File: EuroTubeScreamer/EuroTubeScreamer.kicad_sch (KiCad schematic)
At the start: 49 parts, among them Q1 2N3904, Q2 2N3904, U1 RC4558

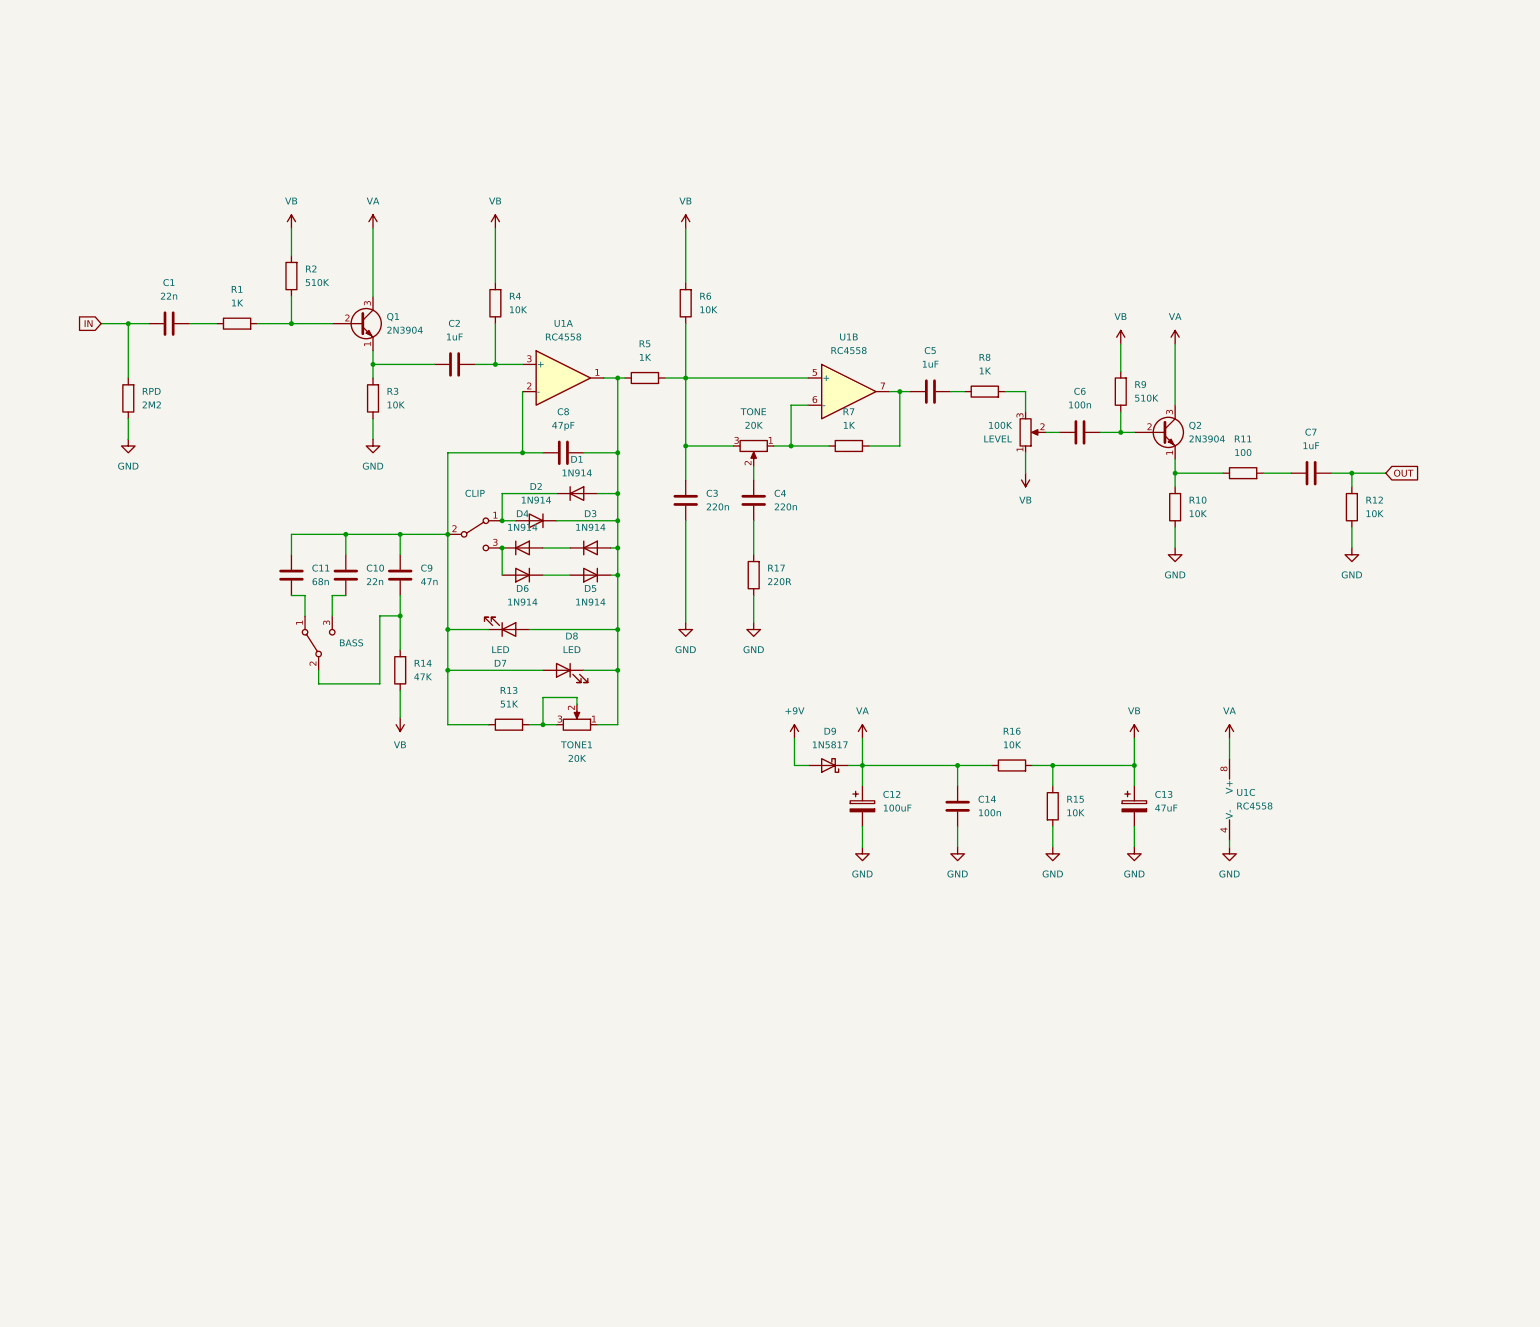
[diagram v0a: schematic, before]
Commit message: added bypass board to schematic and made a start on a panel layout
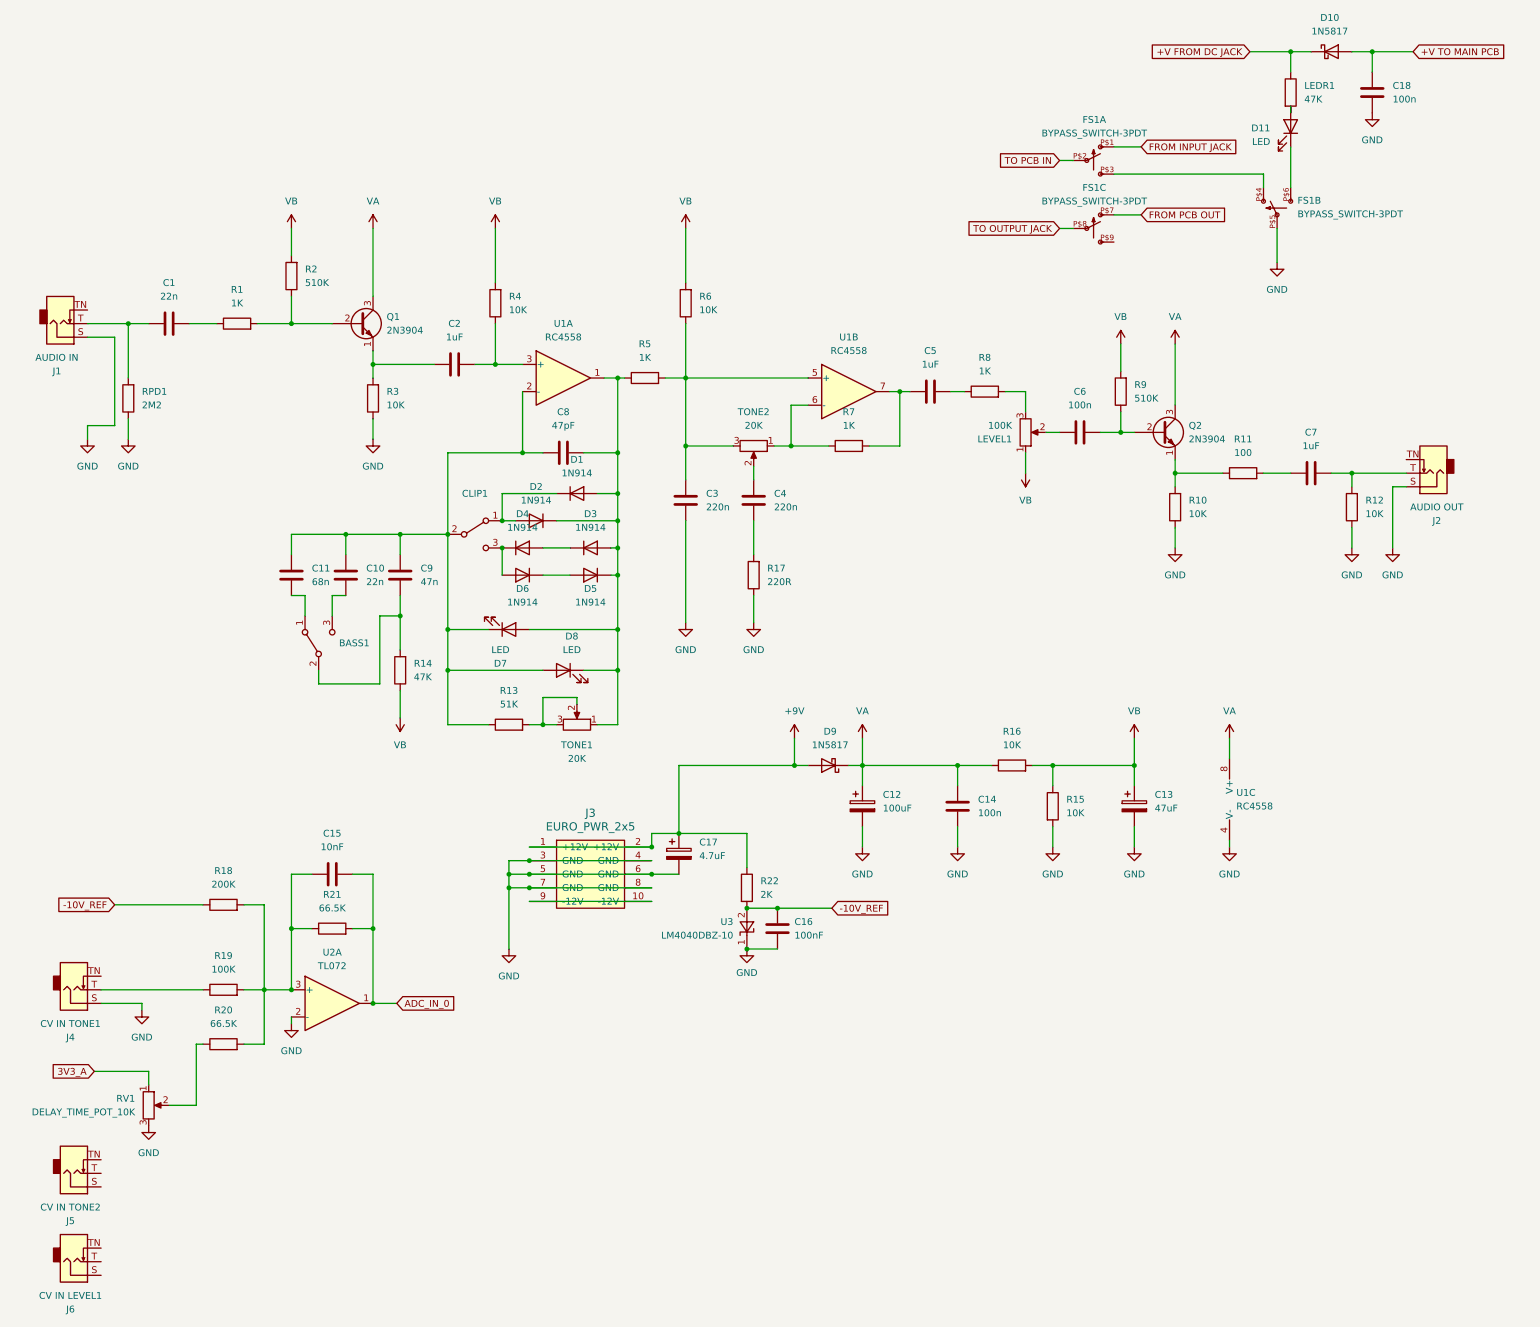
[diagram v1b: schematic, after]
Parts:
- added C15: 10nF, symbol Device:C
- added C16: 100nF, symbol Device:C
- added C17: 4.7uF, Capacitor_THT:CP_Radial_D5.0mm_P2.50mm, symbol Device:C_Polarized
- added C18: 100n, symbol Device:C
- added D10: 1N5817, Diode_THT:D_DO-41_SOD81_P10.16mm_Horizontal, symbol Diode:1N5817
- added D11: LED, LED_THT:LED_D3.0mm, symbol Device:LED
- added FS1: BYPASS_SWITCH-3PDT, SparkFun-Electromechanical:STOMP-SWITCH-3PDT, symbol SparkSparkFun-Electromechanicalfun:SWITCH-3PDT
- added J1: AUDIO IN, eurocad:PJ301M-12_T_S, symbol Connector_Audio:AudioJack2_SwitchT
- added J2: AUDIO OUT, eurocad:PJ301M-12_T_S, symbol Connector_Audio:AudioJack2_SwitchT
- added J3: EURO_PWR_2x5, Connector_IDC:IDC-Header_2x05_P2.54mm_Vertical, symbol eurocad:EURO_PWR_2x5
- added J4: CV IN TONE1, eurocad:PJ301M-12_T_S, symbol Connector_Audio:AudioJack2_SwitchT
- added J5: CV IN TONE2, eurocad:PJ301M-12_T_S, symbol Connector_Audio:AudioJack2_SwitchT
- added J6: CV IN LEVEL1, eurocad:PJ301M-12_T_S, symbol Connector_Audio:AudioJack2_SwitchT
- added LEDR1: 47K, symbol Device:R
- added R18: 200K, symbol Device:R
- added R19: 100K, symbol Device:R
- added R20, R21: 66.5K, symbol Device:R
- added R22: 2K, symbol Device:R
- added RV1: DELAY_TIME_POT_10K, symbol Device:R_Potentiometer
- added U2: TL072, symbol Amplifier_Operational:TL072
- added U3: LM4040DBZ-10, Package_TO_SOT_SMD:SOT-23, symbol Reference_Voltage:LM4040DBZ-10
- BASS1: renamed from BASS; footprint (none) -> Library:ThreeHole_Connector
- CLIP1: renamed from CLIP; footprint (none) -> Library:ThreeHole_Connector
- LEVEL1: renamed from LEVEL; footprint (none) -> eurocad:Alpha9mmPot
- TONE1: footprint (none) -> eurocad:Alpha9mmPot
- TONE2: renamed from TONE; footprint (none) -> eurocad:Alpha9mmPot
- renumbered RPD to RPD1
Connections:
- net +9V: now also C17.1, J3.1 (+12V), J3.2 (+12V), R22.1
- net GND: now also C16.2, C17.2, C18.2, FS1.P$5 (P), J1.S, J2.S, J3.3 (GND), J3.4 (GND), J3.5 (GND), J3.6 (GND), J3.7 (GND), J3.8 (GND), J4.S, RV1.3, U2.2 (-), U3.1 (K)
- net IN: no longer names the net of C1.1, RPD1.2
- net IN: now also J1.T
- net OUT: no longer names the net of C7.2, R12.2
- net OUT: now also J2.T
- new net: D11.2 (A), LEDR1.2
- new net: FS1.P$3 (S), FS1.P$4 (O)
- new net: C15.1, R18.2, R19.2, R20.2, R21.1, U2.3 (+)
- new net: R20.1, RV1.2
- new net: D11.1 (K), FS1.P$6 (S)
- new net: J4.T, R19.1
- new net: J3.10 (-12V), J3.9 (-12V)
- new net +V FROM DC JACK: D10.1 (K), LEDR1.1
- new net +V TO MAIN PCB: C18.1, D10.2 (A)
- new net -10V_REF: C16.1, R18.1, R22.2, U3.2 (A)
- new net 3V3_A: RV1.1
- new net ADC_IN_0: C15.2, R21.2, U2.1
- new net FROM INPUT JACK: FS1.P$1 (O)
- new net FROM PCB OUT: FS1.P$7 (O)
- new net TO OUTPUT JACK: FS1.P$8 (P)
- new net TO PCB IN: FS1.P$2 (P)
